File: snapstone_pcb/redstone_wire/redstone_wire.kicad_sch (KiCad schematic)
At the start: 4 parts

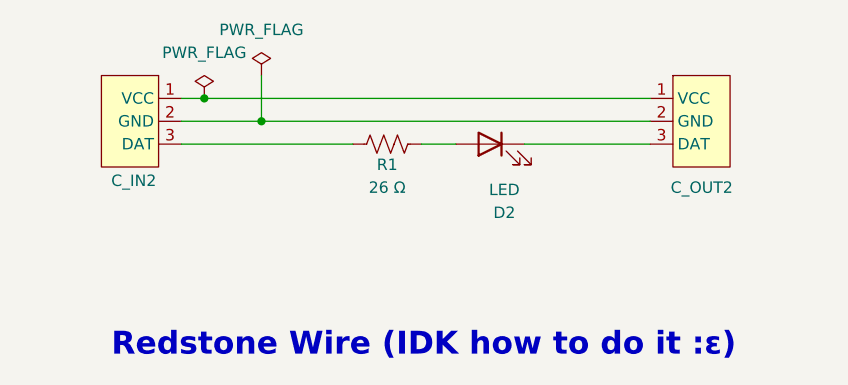
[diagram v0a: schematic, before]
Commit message: Rerouted comparator wires to loop back into connector for inputs #1 and #2... and made some tiny style changes, lol.
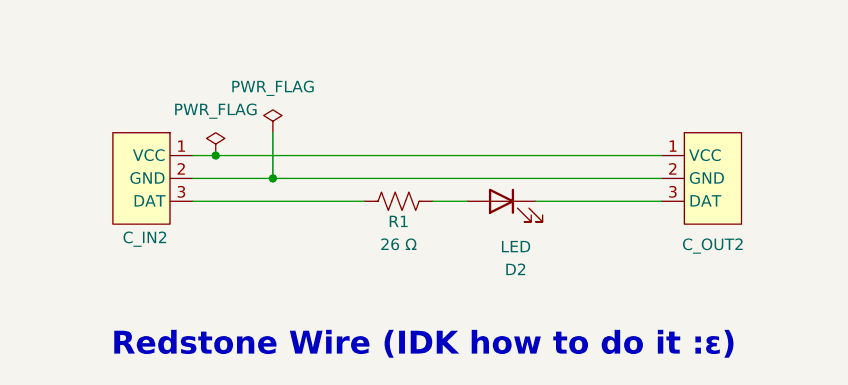
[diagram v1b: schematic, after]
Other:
- moved on the sheet: C_IN2, C_OUT2, D2, R1
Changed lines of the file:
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@@
 	)
 	(junction
-		(at 116.84 71.12)
+		(at 118.11 77.47)
 		(diameter 0)
 		(color 0 0 0 0)
 	)
 	(junction
-		(at 123.19 73.66)
+		(at 124.46 80.01)
 		(diameter 0)
 		(color 0 0 0 0)
@@
 	(wire
 		(pts
-			(xy 114.3 76.2) (xy 133.35 76.2)
-		)
-		(stroke
-			(width 0)
-			(type default)
-		)
-	)
-	(wire
-		(pts
-			(xy 152.4 76.2) (xy 166.37 76.2)
-		)
-		(stroke
-			(width 0)
-			(type default)
-		)
-	)
-	(wire
-		(pts
-			(xy 114.3 73.66) (xy 123.19 73.66)
-		)
-		(stroke
-			(width 0)
-			(type default)
-		)
-	)
-	(wire
-		(pts
-			(xy 114.3 71.12) (xy 116.84 71.12)
-		)
-		(stroke
-			(width 0)
-			(type default)
-		)
-	)
-	(wire
-		(pts
-			(xy 140.97 76.2) (xy 144.78 76.2)
-		)
-		(stroke
-			(width 0)
-			(type default)
-		)
-	)
-	(wire
-		(pts
-			(xy 123.19 68.58) (xy 123.19 73.66)
-		)
-		(stroke
-			(width 0)
-			(type default)
-		)
-	)
-	(wire
-		(pts
-			(xy 116.84 71.12) (xy 166.37 71.12)
-		)
-		(stroke
-			(width 0)
-			(type default)
-		)
-	)
-	(wire
-		(pts
-			(xy 123.19 73.66) (xy 166.37 73.66)
+			(xy 115.57 82.55) (xy 134.62 82.55)
+		)
+		(stroke
+			(width 0)
+			(type default)
+		)
+	)
+	(wire
+		(pts
+			(xy 153.67 82.55) (xy 167.64 82.55)
+		)
+		(stroke
+			(width 0)
+			(type default)
+		)
+	)
+	(wire
+		(pts
+			(xy 115.57 80.01) (xy 124.46 80.01)
+		)
+		(stroke
+			(width 0)
+			(type default)
+		)
+	)
+	(wire
+		(pts
+			(xy 115.57 77.47) (xy 118.11 77.47)
+		)
+		(stroke
+			(width 0)
+			(type default)
+		)
+	)
+	(wire
+		(pts
+			(xy 142.24 82.55) (xy 146.05 82.55)
+		)
+		(stroke
+			(width 0)
+			(type default)
+		)
+	)
+	(wire
+		(pts
+			(xy 124.46 74.93) (xy 124.46 80.01)
+		)
+		(stroke
+			(width 0)
+			(type default)
+		)
+	)
+	(wire
+		(pts
+			(xy 118.11 77.47) (xy 167.64 77.47)
+		)
+		(stroke
+			(width 0)
+			(type default)
+		)
+	)
+	(wire
+		(pts
+			(xy 124.46 80.01) (xy 167.64 80.01)
 		)
 		(stroke
@@
 		(polyline
 			(pts
-				(xy 97.79 60.96) (xy 186.69 60.96) (xy 186.69 93.98) (xy 97.79 93.98)
+				(xy 97.79 64.77) (xy 186.69 64.77) (xy 186.69 93.98) (xy 97.79 93.98)
 			)
 			(stroke
@@
 	(symbol
 		(lib_id "power:PWR_FLAG")
-		(at 116.84 71.12 0)
+		(at 118.11 77.47 0)
 		(mirror y)
 		(unit 1)
@@
 		(dnp no)
 		(property "Reference" "#FLG01"
-			(at 116.84 69.215 0)
+			(at 118.11 75.565 0)
 			(effects
 				(font
@@
 		)
 		(property "Value" "PWR_FLAG"
-			(at 116.84 66.04 0)
-			(effects
-				(font
-					(size 1.27 1.27)
-				)
-			)
-		)
-		(property "Footprint" ""
-			(at 116.84 71.12 0)
+			(at 118.11 72.39 0)
+			(effects
+				(font
+					(size 1.27 1.27)
+				)
+			)
+		)
+		(property "Footprint" ""
+			(at 118.11 77.47 0)
 			(effects
 				(font
@@
 		)
 		(property "Datasheet" "~"
-			(at 116.84 71.12 0)
+			(at 118.11 77.47 0)
 			(effects
 				(font
@@
 		)
 		(property "Description" "Special symbol for telling ERC where power comes from"
-			(at 116.84 71.12 0)
+			(at 118.11 77.47 0)
 			(effects
 				(font
@@
 	(symbol
 		(lib_id "power:PWR_FLAG")
-		(at 123.19 68.58 0)
+		(at 124.46 74.93 0)
 		(mirror y)
 		(unit 1)
@@
 		(dnp no)
 		(property "Reference" "#FLG02"
-			(at 123.19 66.675 0)
+			(at 124.46 73.025 0)
 			(effects
 				(font
@@
 		)
 		(property "Value" "PWR_FLAG"
-			(at 123.19 63.5 0)
-			(effects
-				(font
-					(size 1.27 1.27)
-				)
-			)
-		)
-		(property "Footprint" ""
-			(at 123.19 68.58 0)
+			(at 124.46 69.85 0)
+			(effects
+				(font
+					(size 1.27 1.27)
+				)
+			)
+		)
+		(property "Footprint" ""
+			(at 124.46 74.93 0)
 			(effects
 				(font
@@
 		)
 		(property "Datasheet" "~"
-			(at 123.19 68.58 0)
+			(at 124.46 74.93 0)
 			(effects
 				(font
@@
 		)
 		(property "Description" "Special symbol for telling ERC where power comes from"
-			(at 123.19 68.58 0)
+			(at 124.46 74.93 0)
 			(effects
 				(font
@@
 	(symbol
 		(lib_id "Device:R_US")
-		(at 137.16 76.2 270)
+		(at 138.43 82.55 270)
 		(unit 1)
 		(exclude_from_sim no)
@@
 		(dnp no)
 		(property "Reference" "R1"
-			(at 137.16 78.486 90)
+			(at 138.43 84.836 90)
 			(effects
 				(font
@@
 		)
 		(property "Value" "26 Ω"
-			(at 137.16 81.026 90)
-			(effects
-				(font
-					(size 1.27 1.27)
-				)
-			)
-		)
-		(property "Footprint" ""
-			(at 136.906 77.216 90)
+			(at 138.43 87.376 90)
+			(effects
+				(font
+					(size 1.27 1.27)
+				)
+			)
+		)
+		(property "Footprint" ""
+			(at 138.176 83.566 90)
 			(effects
 				(font
@@
 		)
 		(property "Datasheet" "~"
-			(at 137.16 76.2 0)
+			(at 138.43 82.55 0)
 			(effects
 				(font
@@
 		)
 		(property "Description" "Resistor, US symbol"
-			(at 137.16 76.2 0)
+			(at 138.43 82.55 0)
 			(effects
 				(font
@@
 	(symbol
 		(lib_id "snapstone:3_Pin_Block_Connector")
-		(at 109.22 78.74 0)
+		(at 110.49 85.09 0)
 		(mirror y)
 		(unit 1)
@@
 		(dnp no)
 		(property "Reference" "C_IN2"
-			(at 111.506 80.264 0)
+			(at 112.776 86.614 0)
 			(effects
 				(font
@@
 		)
 		(property "Value" "~"
-			(at 104.14 74.93 0)
+			(at 105.41 81.28 0)
 			(effects
 				(font
@@
 		)
 		(property "Footprint" ""
-			(at 109.22 78.74 0)
+			(at 110.49 85.09 0)
 			(effects
 				(font
@@
 		)
 		(property "Datasheet" ""
-			(at 109.22 78.74 0)
+			(at 110.49 85.09 0)
 			(effects
 				(font
@@
 		)
 		(property "Description" ""
-			(at 109.22 78.74 0)
+			(at 110.49 85.09 0)
 			(effects
 				(font
@@
 	(symbol
 		(lib_id "snapstone:3_Pin_Block_Connector")
-		(at 171.45 78.74 0)
+		(at 172.72 85.09 0)
 		(unit 1)
 		(exclude_from_sim no)
@@
 		(dnp no)
 		(property "Reference" "C_OUT2"
-			(at 168.656 81.026 0)
+			(at 169.926 87.376 0)
 			(effects
 				(font
@@
 		)
 		(property "Value" "~"
-			(at 176.53 74.93 0)
+			(at 177.8 81.28 0)
 			(effects
 				(font
@@
 		)
 		(property "Footprint" ""
-			(at 171.45 78.74 0)
+			(at 172.72 85.09 0)
 			(effects
 				(font
@@
 		)
 		(property "Datasheet" ""
-			(at 171.45 78.74 0)
+			(at 172.72 85.09 0)
 			(effects
 				(font
@@
 		)
 		(property "Description" ""
-			(at 171.45 78.74 0)
+			(at 172.72 85.09 0)
 			(effects
 				(font
@@
 	(symbol
 		(lib_id "Device:LED")
-		(at 148.59 76.2 0)
+		(at 149.86 82.55 0)
 		(mirror y)
 		(unit 1)
@@
 		(fields_autoplaced yes)
 		(property "Reference" "D2"
-			(at 150.1775 83.82 0)
+			(at 151.4475 90.17 0)
 			(effects
 				(font
@@
 		)
 		(property "Value" "LED"
-			(at 150.1775 81.28 0)
-			(effects
-				(font
-					(size 1.27 1.27)
-				)
-			)
-		)
-		(property "Footprint" ""
-			(at 148.59 76.2 0)
+			(at 151.4475 87.63 0)
+			(effects
+				(font
+					(size 1.27 1.27)
+				)
+			)
+		)
+		(property "Footprint" ""
+			(at 149.86 82.55 0)
 			(effects
 				(font
@@
 		)
 		(property "Datasheet" "~"
-			(at 148.59 76.2 0)
+			(at 149.86 82.55 0)
 			(effects
 				(font
@@
 		)
 		(property "Description" "Light emitting diode"
-			(at 148.59 76.2 0)
+			(at 149.86 82.55 0)
 			(effects
 				(font
@@
 		)
 		(property "Sim.Pins" "1=K 2=A"
-			(at 148.59 76.2 0)
-			(effects
-				(font
+			(at 149.86 82.55 0)
+			(effects
+				(font

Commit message: Updated resistor footprint project-wide
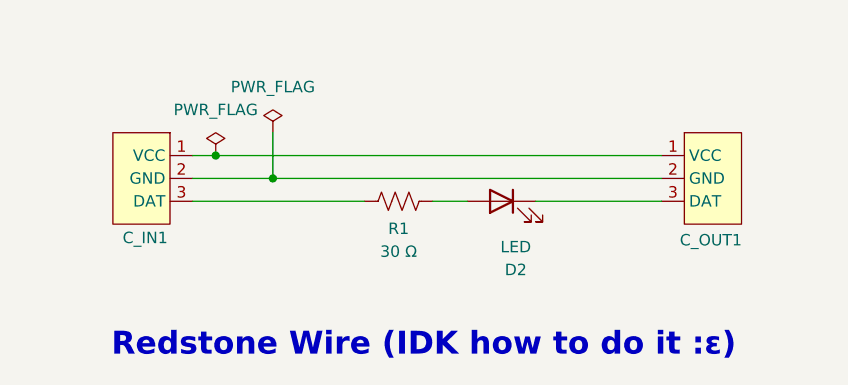
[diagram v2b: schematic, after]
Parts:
- C_IN1: renamed from C_IN2; value ~ -> (none); footprint (none) -> 691137710003_Board_To_Wire:691137710003_Board_To_Wire
- C_OUT1: renamed from C_OUT2; value ~ -> (none); footprint (none) -> 691137710003_Board_To_Wire:691137710003_Board_To_Wire
- R1: value 26 Ω -> 30 Ω; footprint (none) -> CF12JT_Resistor:STA_CF12_STP
